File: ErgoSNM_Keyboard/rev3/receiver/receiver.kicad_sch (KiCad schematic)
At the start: 33 parts, among them J1 Conn_01x13, J2 Conn_01x13, J3 Conn_01x04, J4 Conn_02x05_Counter_Clockwise, J5 Conn_01x04, SW1 RESET, U1 E73-2G4M08S1C, Y1 32.768kHz

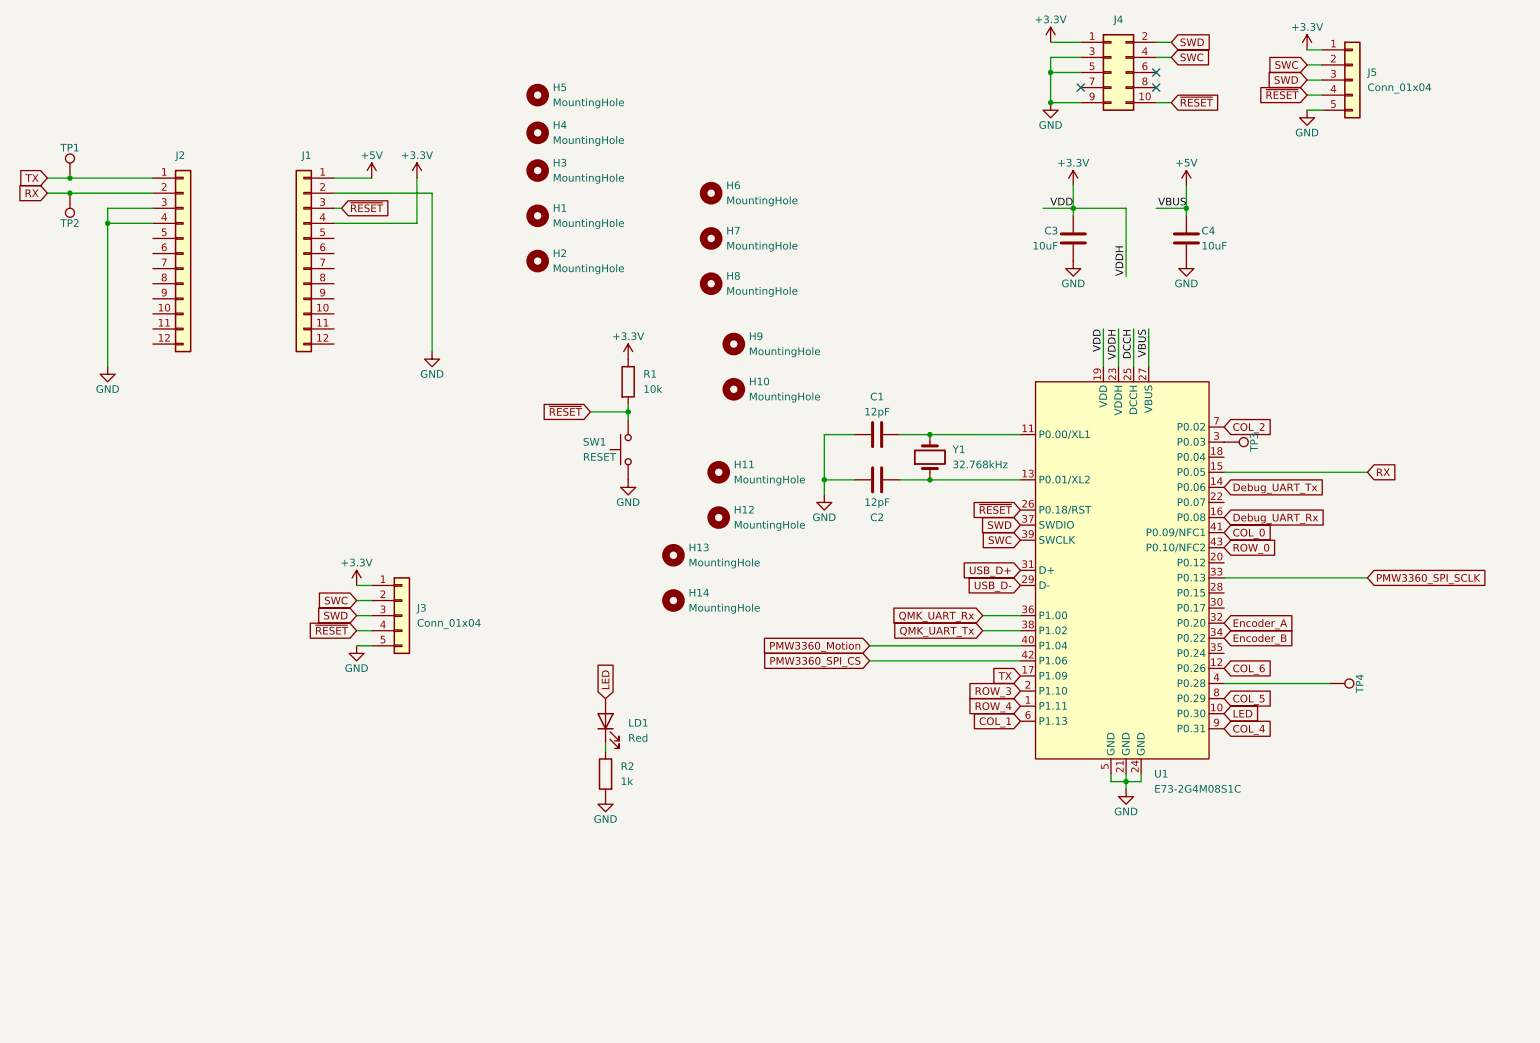
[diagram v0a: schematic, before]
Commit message: Change license to CERN-OHL-P v2
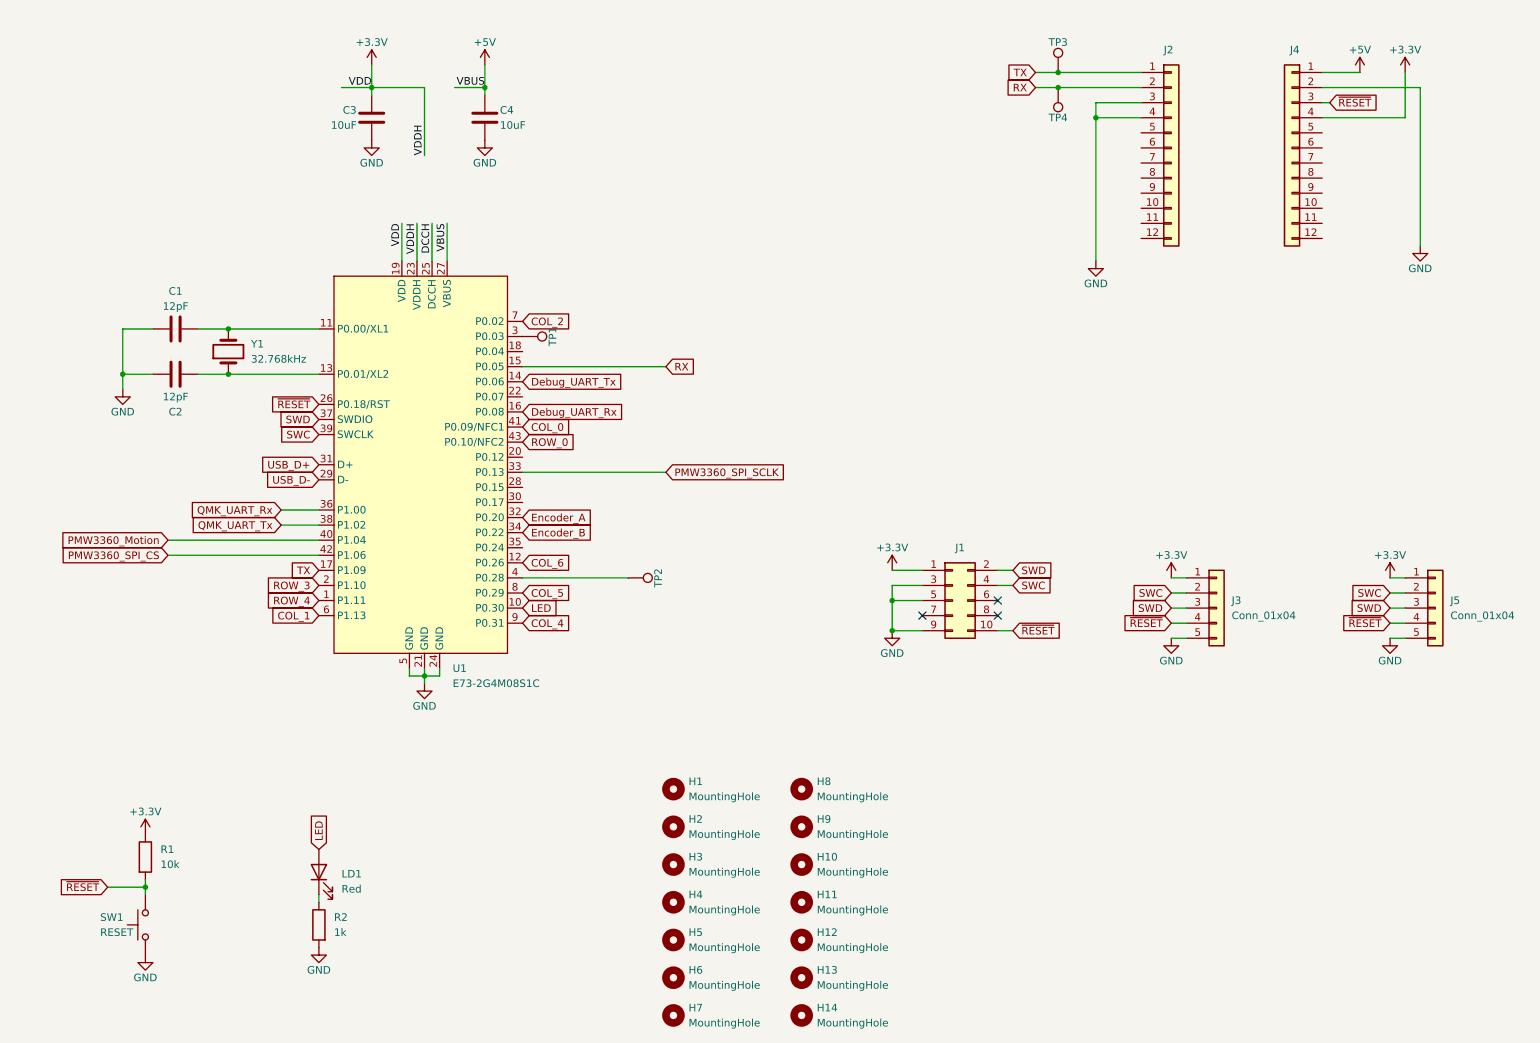
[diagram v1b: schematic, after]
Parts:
- renumbered H5 to H1, H8 to H10, H9 to H11, H10 to H12, H11 to H13, H12 to H14, H4 to H2, H1 to H4, H2 to H5, H13 to H6, H14 to H7, H6 to H8, H7 to H9, J4 to J1, J5 to J3, J1 to J4, J3 to J5, TP3 to TP1, TP4 to TP2, TP1 to TP3, TP2 to TP4
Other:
- moved on the sheet: C1, C2, C3, C4, H1, H10, H11, H12, H13, H14, H2, H3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
